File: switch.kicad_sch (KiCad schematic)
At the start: 3 parts

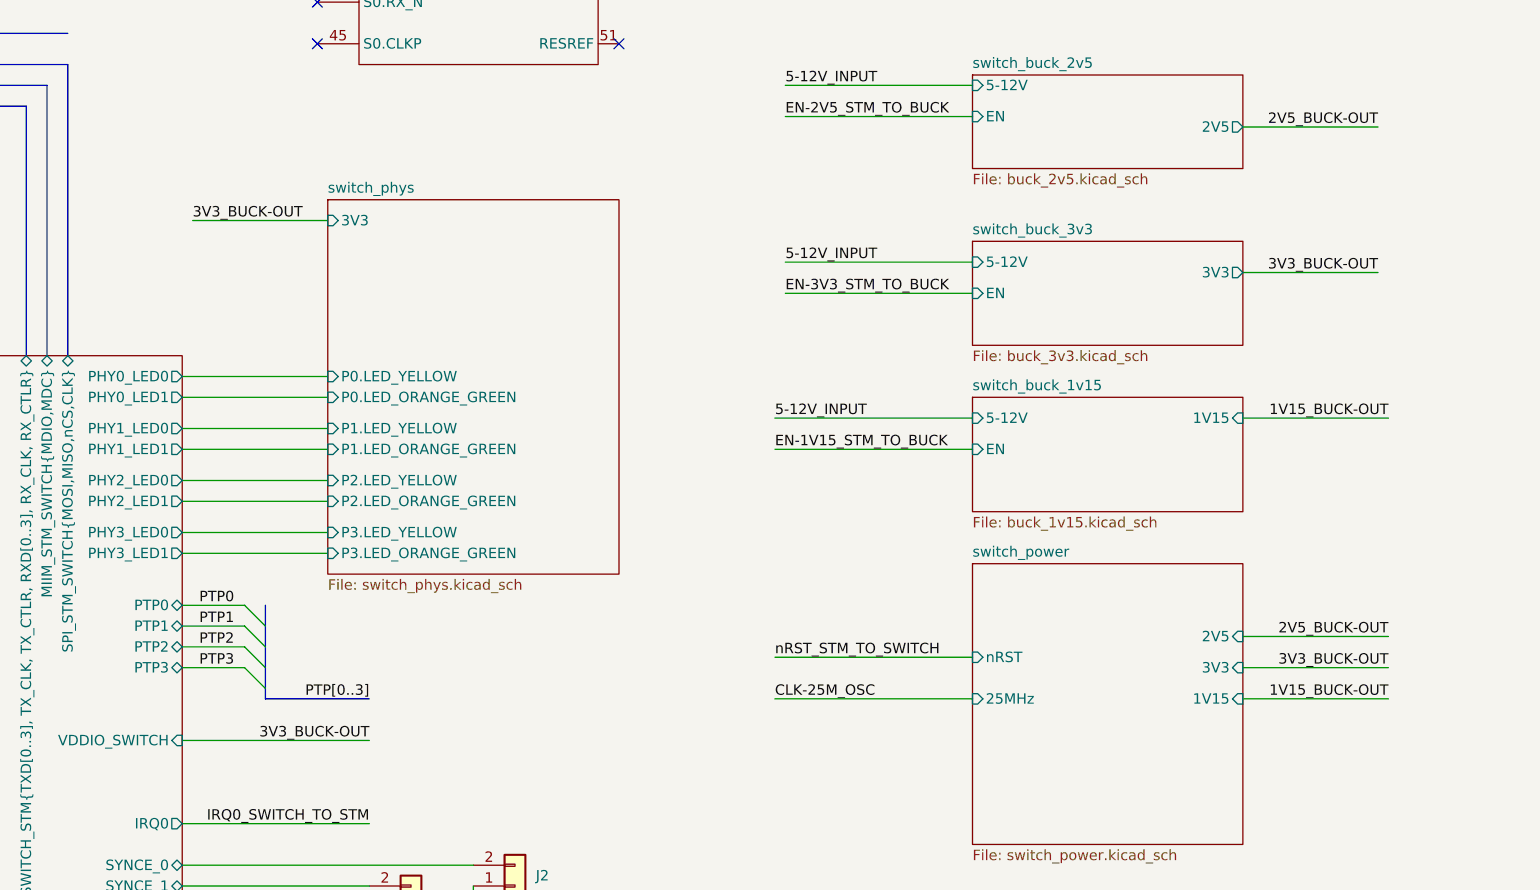
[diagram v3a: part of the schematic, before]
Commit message: moves +3V3 converter to root. Refs: #1
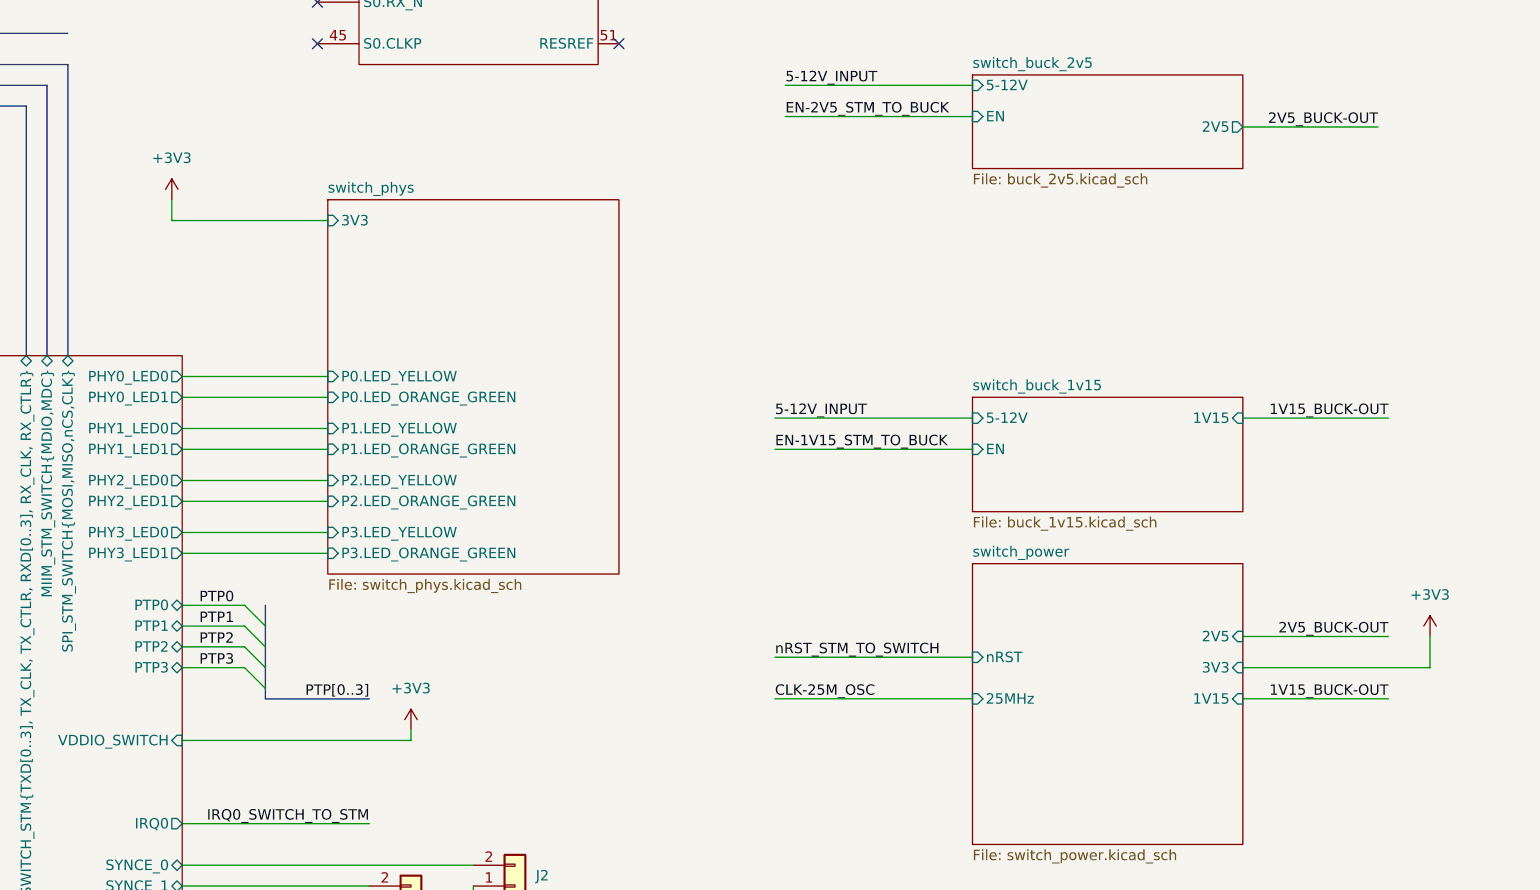
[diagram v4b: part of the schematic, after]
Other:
- removed sheet switch_buck_3v3
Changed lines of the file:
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@@
 	(wire
 		(pts
-			(xy 116.84 139.7) (xy 139.7 139.7)
-		)
-		(stroke
-			(width 0)
-			(type default)
-		)
-	)
-	(wire
-		(pts
-			(xy 190.5 85.09) (xy 213.36 85.09)
+			(xy 116.84 139.7) (xy 144.78 139.7)
+		)
+		(stroke
+			(width 0)
+			(type default)
+		)
+	)
+	(wire
+		(pts
+			(xy 115.57 73.66) (xy 115.57 76.2)
 		)
 		(stroke
@@
 	(wire
 		(pts
-			(xy 190.5 81.28) (xy 213.36 81.28)
-		)
-		(stroke
-			(width 0)
-			(type default)
-		)
-	)
-	(wire
-		(pts
 			(xy 116.84 157.48) (xy 139.7 157.48)
 		)
@@
 	(wire
 		(pts
-			(xy 246.38 130.81) (xy 264.16 130.81)
+			(xy 246.38 130.81) (xy 269.24 130.81)
 		)
 		(stroke
@@
 	(wire
 		(pts
-			(xy 118.11 76.2) (xy 134.62 76.2)
-		)
-		(stroke
-			(width 0)
-			(type default)
-		)
-	)
-	(wire
-		(pts
 			(xy 189.23 104.14) (xy 213.36 104.14)
 		)
@@
 	(wire
 		(pts
-			(xy 246.38 82.55) (xy 262.89 82.55)
-		)
-		(stroke
-			(width 0)
-			(type default)
-		)
-	)
-	(wire
-		(pts
 			(xy 116.84 125.73) (xy 124.46 125.73)
 		)
@@
 	(wire
 		(pts
+			(xy 115.57 76.2) (xy 134.62 76.2)
+		)
+		(stroke
+			(width 0)
+			(type default)
+		)
+	)
+	(wire
+		(pts
 			(xy 72.39 21.59) (xy 96.52 21.59)
 		)
@@
 	(wire
 		(pts
+			(xy 144.78 139.7) (xy 144.78 138.43)
+		)
+		(stroke
+			(width 0)
+			(type default)
+		)
+	)
+	(wire
+		(pts
 			(xy 72.39 43.18) (xy 96.52 43.18)
 		)
@@
 		(pts
 			(xy 116.84 149.86) (xy 139.7 149.86)
+		)
+		(stroke
+			(width 0)
+			(type default)
+		)
+	)
+	(wire
+		(pts
+			(xy 269.24 127) (xy 269.24 130.81)
 		)
 		(stroke
@@
 		)
 	)
-	(label "EN-3V3_STM_TO_BUCK"
-		(at 190.5 85.09 0)
-		(effects
-			(font
-				(size 1.27 1.27)
-			)
-			(justify left bottom)
-		)
-	)
 	(label "PTP0"
 		(at 123.19 123.19 180)
@@
 		)
 	)
-	(label "3V3_BUCK-OUT"
-		(at 118.11 76.2 0)
-		(effects
-			(font
-				(size 1.27 1.27)
-			)
-			(justify left bottom)
-		)
-	)
 	(label "EN-3V3_STM_TO_BUCK"
 		(at 96.52 35.56 180)
@@
 		)
 	)
-	(label "3V3_BUCK-OUT"
-		(at 264.16 130.81 180)
-		(effects
-			(font
-				(size 1.27 1.27)
-			)
-			(justify right bottom)
-		)
-	)
 	(label "EN-2V5_STM_TO_BUCK"
 		(at 190.5 63.5 0)
@@
 		)
 	)
-	(label "3V3_BUCK-OUT"
-		(at 262.89 82.55 180)
-		(effects
-			(font
-				(size 1.27 1.27)
-			)
-			(justify right bottom)
-		)
-	)
-	(label "5-12V_INPUT"
-		(at 190.5 81.28 0)
-		(effects
-			(font
-				(size 1.27 1.27)
-			)
-			(justify left bottom)
-		)
-	)
 	(label "5-12V_INPUT"
 		(at 189.23 100.33 0)
@@
 	(label "IRQ0_SWITCH_TO_STM"
 		(at 139.7 149.86 180)
-		(effects
-			(font
-				(size 1.27 1.27)
-			)
-			(justify right bottom)
-		)
-	)
-	(label "3V3_BUCK-OUT"
-		(at 139.7 139.7 180)
 		(effects
 			(font
@@
 	)
 	(symbol
+		(lib_id "power:+3V3")
+		(at 269.24 127 0)
+		(unit 1)
+		(exclude_from_sim no)
+		(in_bom yes)
+		(on_board yes)
+		(dnp no)
+		(fields_autoplaced yes)
+		(property "Reference" "#PWR088"
+			(at 269.24 130.81 0)
+			(effects
+				(font
+					(size 1.27 1.27)
+				)
+				(hide yes)
+			)
+		)
+		(property "Value" "+3V3"
+			(at 269.24 121.92 0)
+			(effects
+				(font
+					(size 1.27 1.27)
+				)
+			)
+		)
+		(property "Footprint" ""
+			(at 269.24 127 0)
+			(effects
+				(font
+					(size 1.27 1.27)
+				)
+				(hide yes)
+			)
+		)
+		(property "Datasheet" ""
+			(at 269.24 127 0)
+			(effects
+				(font
+					(size 1.27 1.27)
+				)
+				(hide yes)
+			)
+		)
+		(property "Description" "Power symbol creates a global label with name \"+3V3\""
+			(at 269.24 127 0)
+			(effects
+				(font
+					(size 1.27 1.27)
+				)
+				(hide yes)
+			)
+		)
+		(pin "1"
+		)
+		(instances
+			(project ""
+				(path "/d4536448-b109-4159-96e2-3dc21baf2d6e/0b7d9af9-83c1-43fa-a7a0-a33d0a00ea9c"
+					(reference "#PWR088")
+					(unit 1)
+				)
+			)
+		)
+	)
+	(symbol
+		(lib_id "power:+3V3")
+		(at 115.57 73.66 0)
+		(unit 1)
+		(exclude_from_sim no)
+		(in_bom yes)
+		(on_board yes)
+		(dnp no)
+		(fields_autoplaced yes)
+		(property "Reference" "#PWR090"
+			(at 115.57 77.47 0)
+			(effects
+				(font
+					(size 1.27 1.27)
+				)
+				(hide yes)
+			)
+		)
+		(property "Value" "+3V3"
+			(at 115.57 68.58 0)
+			(effects
+				(font
+					(size 1.27 1.27)
+				)
+			)
+		)
+		(property "Footprint" ""
+			(at 115.57 73.66 0)
+			(effects
+				(font
+					(size 1.27 1.27)
+				)
+				(hide yes)
+			)
+		)
+		(property "Datasheet" ""
+			(at 115.57 73.66 0)
+			(effects
+				(font
+					(size 1.27 1.27)
+				)
+				(hide yes)
+			)
+		)
+		(property "Description" "Power symbol creates a global label with name \"+3V3\""
+			(at 115.57 73.66 0)
+			(effects
+				(font
+					(size 1.27 1.27)
+				)
+				(hide yes)
+			)
+		)
+		(pin "1"
+		)
+		(instances
+			(project ""
+				(path "/d4536448-b109-4159-96e2-3dc21baf2d6e/0b7d9af9-83c1-43fa-a7a0-a33d0a00ea9c"
+					(reference "#PWR090")
+					(unit 1)
+				)
+			)
+		)
+	)
+	(symbol
+		(lib_id "power:+3V3")
+		(at 144.78 138.43 0)
+		(unit 1)
+		(exclude_from_sim no)
+		(in_bom yes)
+		(on_board yes)
+		(dnp no)
+		(fields_autoplaced yes)
+		(property "Reference" "#PWR089"
+			(at 144.78 142.24 0)
+			(effects
+				(font
+					(size 1.27 1.27)
+				)
+				(hide yes)
+			)
+		)
+		(property "Value" "+3V3"
+			(at 144.78 133.35 0)
+			(effects
+				(font
+					(size 1.27 1.27)
+				)
+			)
+		)
+		(property "Footprint" ""
+			(at 144.78 138.43 0)
+			(effects
+				(font
+					(size 1.27 1.27)
+				)
+				(hide yes)
+			)
+		)
+		(property "Datasheet" ""
+			(at 144.78 138.43 0)
+			(effects
+				(font
+					(size 1.27 1.27)
+				)
+				(hide yes)
+			)
+		)
+		(property "Description" "Power symbol creates a global label with name \"+3V3\""
+			(at 144.78 138.43 0)
+			(effects
+				(font
+					(size 1.27 1.27)
+				)
+				(hide yes)
+			)
+		)
+		(pin "1"
+		)
+		(instances
+			(project ""
+				(path "/d4536448-b109-4159-96e2-3dc21baf2d6e/0b7d9af9-83c1-43fa-a7a0-a33d0a00ea9c"
+					(reference "#PWR089")
+					(unit 1)
+				)
+			)
+		)
+	)
+	(symbol
 		(lib_id "KL_SYM_LOCAL:GND")
 		(at 152.4 161.29 0)
@@
 				)
 			)
-		)
-	)
-	(sheet
-		(at 213.36 78.74)
-		(size 33.02 12.7)
-		(exclude_from_sim no)
-		(in_bom yes)
-		(on_board yes)
-		(dnp no)
-		(fields_autoplaced yes)
-		(stroke
-			(width 0.1524)
-			(type solid)
-		)
-		(fill
-			(color 0 0 0 0.0000)
-		)
-		(property "Sheetname" "switch_buck_3v3"
-			(at 213.36 78.0284 0)
-			(effects
-				(font
-					(size 1.27 1.27)
-				)
-				(justify left bottom)
-			)
-		)
-		(property "Sheetfile" "buck_3v3.kicad_sch"
-			(at 213.36 92.0246 0)
-			(effects
-				(font
-					(size 1.27 1.27)
-				)
-				(justify left top)
-			)
-		)
-		(pin "3V3" output
-			(at 246.38 82.55 0)
-			(effects
-				(font
-					(size 1.27 1.27)
-				)
-				(justify right)
-			)
-		)
-		(pin "5-12V" input
-			(at 213.36 81.28 180)
-			(effects
-				(font
-					(size 1.27 1.27)
-				)
-				(justify left)
-			)
-		)
-		(pin "EN" input
-			(at 213.36 85.09 180)
-			(effects
-				(font
-					(size 1.27 1.27)
-				)
-				(justify left)
-			)
-		)
-		(instances
-			(project "shish-lan"
-				(path "/d4536448-b109-4159-96e2-3dc21baf2d6e/0b7d9af9-83c1-43fa-a7a0-a33d0a00ea9c"
-					(page "5")
-				)
-			)
-			(project "switch"
-				(path "/cd936d40-9035-4ec8-bcf8-38758f995fb0"
-					(page "5")
-				)
-			)

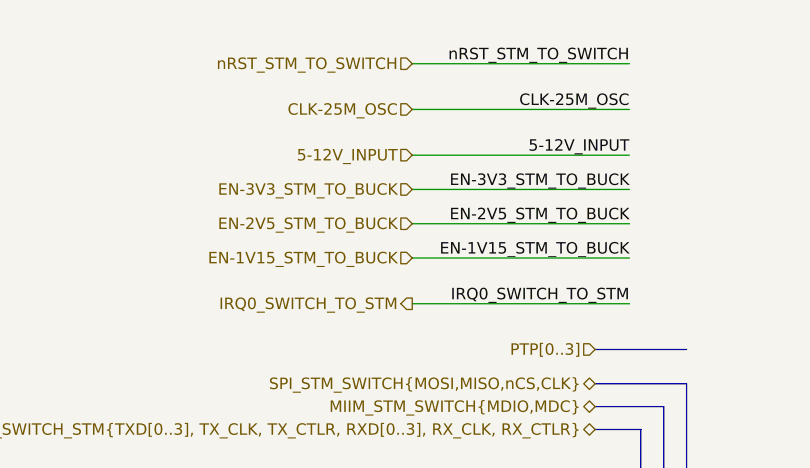
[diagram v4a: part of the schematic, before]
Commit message: connects 1V15 and 2V5 to STM. Refs: #1
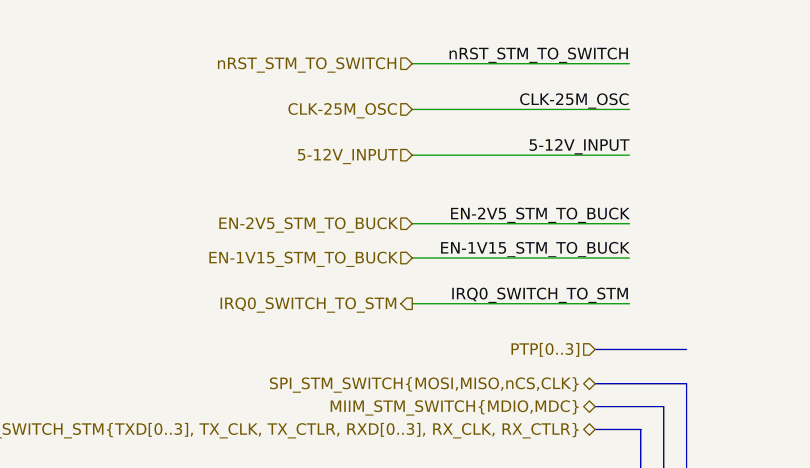
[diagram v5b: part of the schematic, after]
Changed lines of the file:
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@@
-	(wire
-		(pts
-			(xy 72.39 35.56) (xy 96.52 35.56)
-		)
-		(stroke
-			(width 0)
-			(type default)
-		)
-	)
 	(wire
 		(pts
@@
 	(label "nRST_STM_TO_SWITCH"
 		(at 96.52 21.59 180)
-		(effects
-			(font
-				(size 1.27 1.27)
-			)
-			(justify right bottom)
-		)
-	)
-	(label "EN-3V3_STM_TO_BUCK"
-		(at 96.52 35.56 180)
 		(effects
 			(font
@@
 		(effects
 			(font
-				(size 1.27 1.27)
-			)
-			(justify right)
-		)
-	)
-	(hierarchical_label "EN-3V3_STM_TO_BUCK"
-		(shape input)
-		(at 72.39 35.56 180)
-		(effects
-			(font

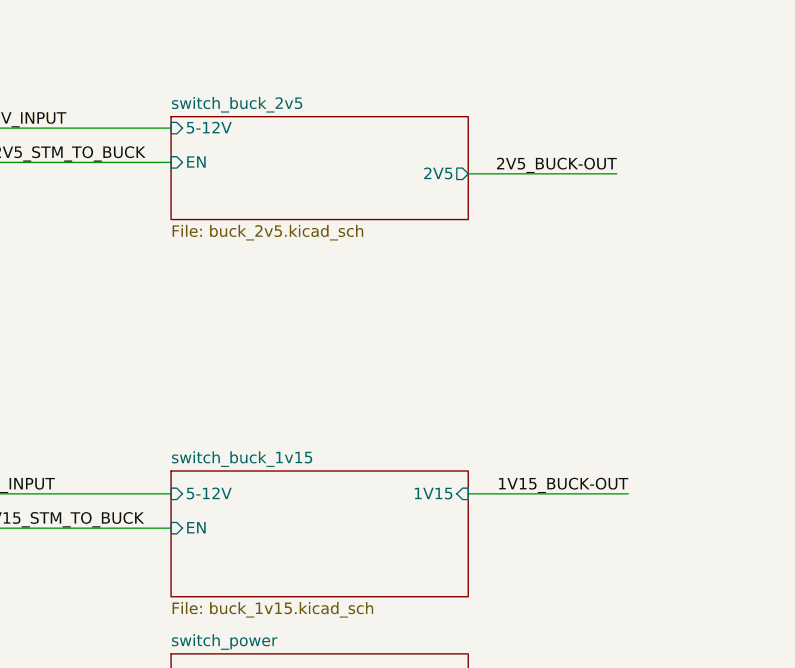
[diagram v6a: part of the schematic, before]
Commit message: fixes ERC errors in DC/DC converters
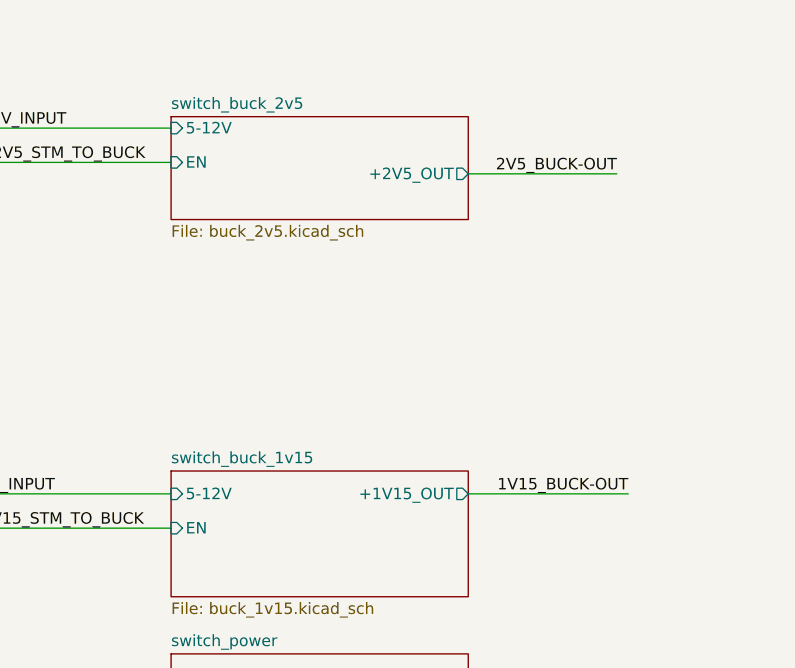
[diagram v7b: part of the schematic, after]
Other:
- sheet switch_buck_1v15 ports: added +1V15_OUT; removed 1V15
- sheet switch_buck_2v5 ports: added +2V5_OUT; removed 2V5
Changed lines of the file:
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@@
 			)
 		)
-		(pin "1V15" input
+		(pin "+1V15_OUT" output
 			(at 246.38 100.33 0)
 			(effects
@@
 			)
 		)
-		(pin "2V5" output
+		(pin "+2V5_OUT" output
 			(at 246.38 64.77 0)
 			(effects

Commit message: updates pin headers
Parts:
- J2, J3: footprint KL:02x01_2.54mm_Header -> KL_Footprints:02x01_2.54mm_Header
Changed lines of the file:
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@@
 		(dnp no)
 		(property "Reference" "J2"
-			(at 160.02 156.2101 0)
+			(at 157.226 159.766 0)
 			(effects
 				(font
 					(size 1.27 1.27)
 				)
-				(justify left)
 			)
 		)
@@
 			)
 		)
-		(property "Footprint" "KL:02x01_2.54mm_Header"
+		(property "Footprint" "KL_Footprints:02x01_2.54mm_Header"
 			(at 157.48 156.21 0)
 			(effects
@@
 		(dnp no)
 		(property "Reference" "J3"
-			(at 147.32 158.7501 0)
+			(at 144.526 162.306 0)
 			(effects
 				(font
 					(size 1.27 1.27)
 				)
-				(justify left)
 			)
 		)
@@
 			)
 		)
-		(property "Footprint" "KL:02x01_2.54mm_Header"
+		(property "Footprint" "KL_Footprints:02x01_2.54mm_Header"
 			(at 144.78 158.75 0)
 			(effects
